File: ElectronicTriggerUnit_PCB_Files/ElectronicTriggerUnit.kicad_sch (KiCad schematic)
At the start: 36 parts, among them IC3 ATTINY816-MNR, J4 Conn_01x04, Q1 LC191PTDT, Q2 LKPT30102B-A01, Q3 78-SQRS140ELP, Q4 LC191PTDT, Q5 2N7002, Q8 SI7149ADP-T1-GE3, U2 12v, U3 GndMotor, U4 Gnd, U5 LM1117MP-5.0

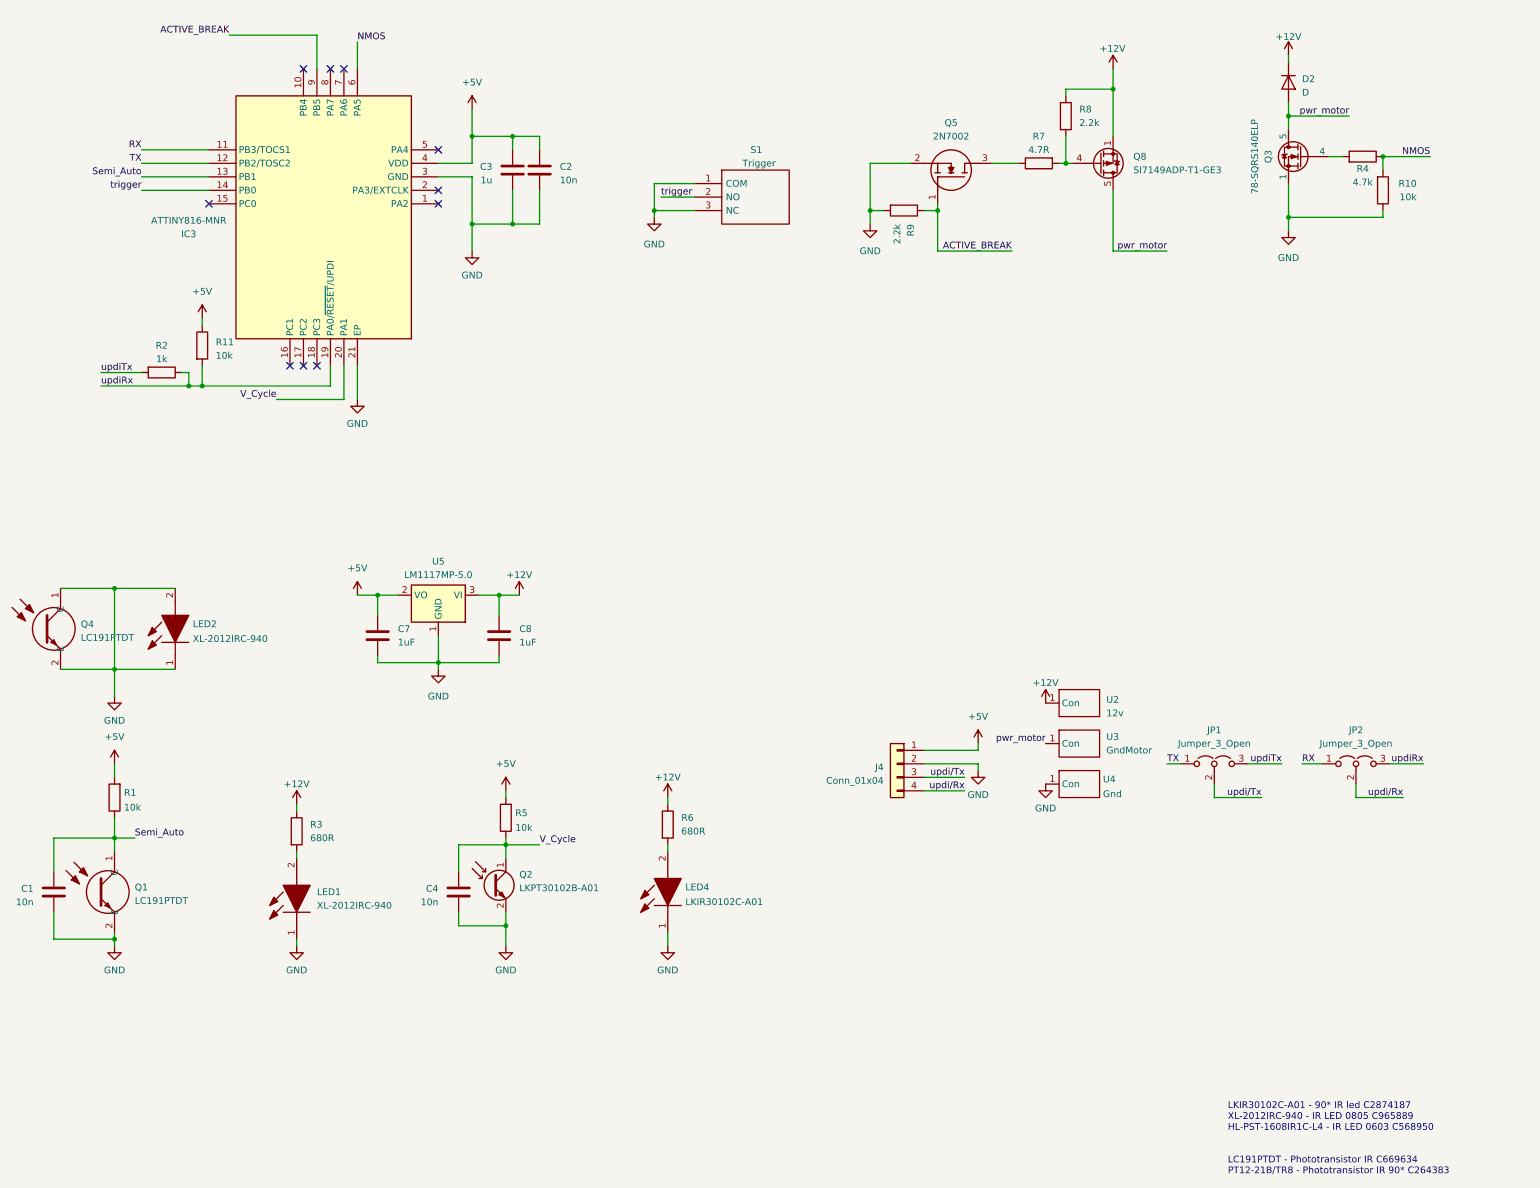
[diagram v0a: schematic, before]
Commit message: modular board version
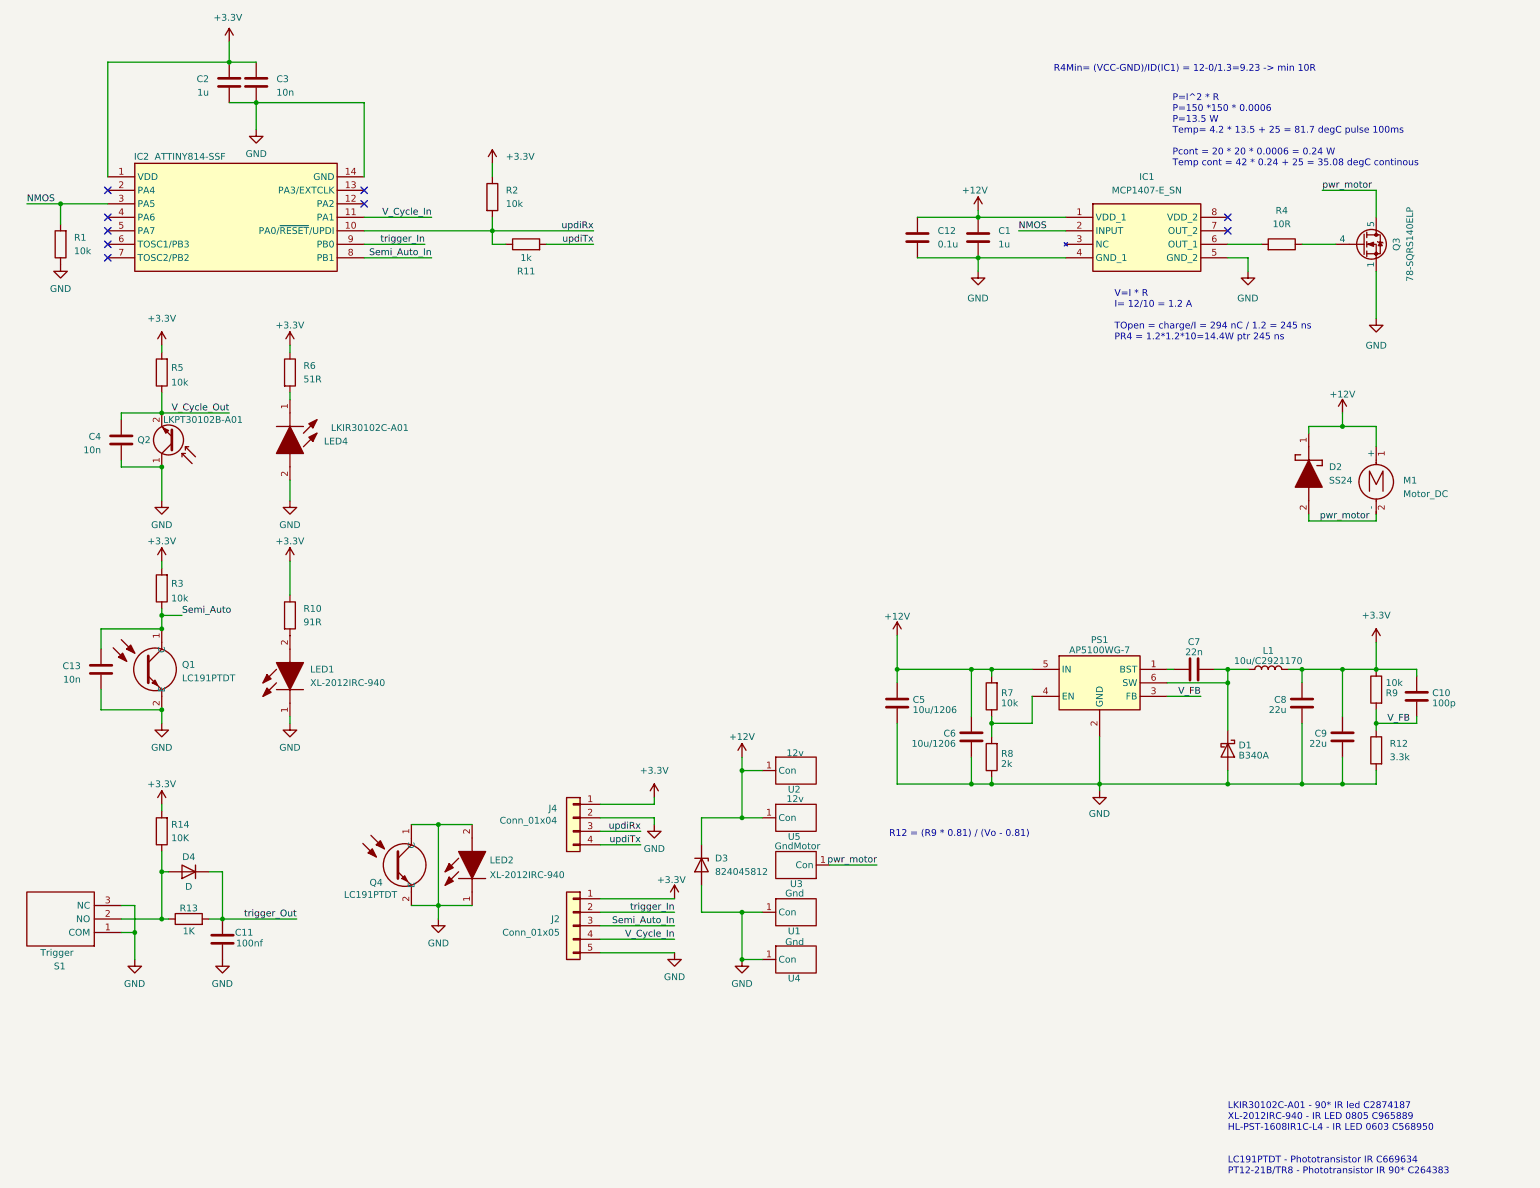
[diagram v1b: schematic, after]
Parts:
- removed D2: D, SamacSys_Parts:SBR3U60P1Q7, symbol Device:D
- removed IC3: ATTINY816-MNR, SamacSys_Parts:QFN40P300X300X90-21N, symbol SamacSys_Parts:ATTINY816-MNR
- removed JP1, JP2: Jumper_3_Open, Jumper:SolderJumper-3_P1.3mm_Open_RoundedPad1.0x1.5mm, symbol Jumper:Jumper_3_Open
- removed Q5: 2N7002, SOT96P240X120-3N, symbol SamacSys_Parts:2N7002
- removed Q8: SI7149ADP-T1-GE3, SamacSys_Parts:POWERPAKSO-8, symbol Transistor_FET:Si7141DP
- removed U5: LM1117MP-5.0, Package_TO_SOT_SMD:SOT-223-3_TabPin2, symbol Regulator_Linear:LM1117MP-5.0
- added C10: 100p, Capacitor_SMD:C_0603_1608Metric, symbol Device:C
- added C11: 100nf, Capacitor_SMD:C_0603_1608Metric, symbol Device:C
- added C12: 0.1u, Capacitor_SMD:C_0603_1608Metric, symbol Device:C
- added C13: 10n, Capacitor_SMD:C_0603_1608Metric, symbol Device:C
- added C5, C6: 10u/1206, Capacitor_SMD:C_0603_1608Metric, symbol Device:C
- added C9: 22u, Capacitor_SMD:C_0603_1608Metric, symbol Device:C
- added D1: B340A, Diode_SMD:D_SMA, symbol Device:D_Schottky
- added D2: SS24, SamacSys:DIOM5436X247N, symbol SamacSys:SS24
- added D3: 824045812, SamacSys:TVS_DIODE, symbol Diode:ESD5Zxx
- added D4: D, Diode_SMD:D_0603_1608Metric, symbol Device:D
- added IC1: MCP1407-E_SN, SamacSys:SOIC127P600X175-8N, symbol SamacSys:MCP1407-E_SN
- added IC2: ATTINY814-SSF, SamacSys:SOIC127P600X175-14N, symbol SamacSys:ATTINY814-SSF
- added J2: Conn_01x05, Connector_PinSocket_2.54mm:PinSocket_1x05_P2.54mm_Vertical, symbol Connector_Generic:Conn_01x05
- added L1: 10u/C2921170, Inductor_SMD:L_Chilisin_BMRA00040420, symbol Device:L
- added M1: Motor_DC, symbol Motor:Motor_DC
- added PS1: AP5100WG-7, SamacSys:SOT95P285X140-6N, symbol SamacSys_Parts:AP5100WG-7
- added R12: 3.3k, Resistor_SMD:R_0603_1608Metric, symbol Device:R
- added R13: 1K, Resistor_SMD:R_0603_1608Metric, symbol Device:R
- added R14: 10K, Resistor_SMD:R_0603_1608Metric, symbol Device:R
- added U1: Gnd, SamacSys:Copper_Pad, symbol Copper_Pad:Copper_pad
- added U5: 12v, SamacSys:Copper_Pad, symbol Copper_Pad:Copper_pad
- C1, C2: value 10n -> 1u; footprint Capacitor_SMD:C_0402_1005Metric -> Capacitor_SMD:C_0603_1608Metric
- C3: value 1u -> 10n; footprint Capacitor_SMD:C_0402_1005Metric -> Capacitor_SMD:C_0603_1608Metric
- C4: footprint Capacitor_SMD:C_0402_1005Metric -> Capacitor_SMD:C_0603_1608Metric
- C7: value 1uF -> 22n; footprint Capacitor_SMD:C_0402_1005Metric -> Capacitor_SMD:C_0603_1608Metric; MPN (none) -> C21122
- C8: value 1uF -> 22u; footprint Capacitor_SMD:C_0402_1005Metric -> Capacitor_SMD:C_0603_1608Metric; MPN (none) -> C45783
- LED1, LED2: footprint SamacSys_Parts:LEDC2012X105N -> SamacSys:LEDC2012X105N
- LED4, Q2: footprint SamacSys_Parts:APA3010P3C -> SamacSys:APA3010P3C
- Q1, Q4: footprint SamacSys_Parts:AP1608P1CP22 -> SamacSys:AP1608P1CP22
- Q3: footprint SamacSys_Parts:POWERPAKSO-8 -> SamacSys:POWERPAKSO-8
- R1, R5: footprint Resistor_SMD:R_0402_1005Metric -> Resistor_SMD:R_0603_1608Metric
- R10: value 10k -> 91R; footprint Resistor_SMD:R_0402_1005Metric -> Resistor_SMD:R_0603_1608Metric
- R11: value 10k -> 1k; footprint Resistor_SMD:R_0402_1005Metric -> Resistor_SMD:R_0603_1608Metric
- R2: value 1k -> 10k; footprint Resistor_SMD:R_0402_1005Metric -> Resistor_SMD:R_0603_1608Metric
- R3: value 680R -> 10k; footprint Resistor_SMD:R_0402_1005Metric -> Resistor_SMD:R_0603_1608Metric
- R4: value 4.7k -> 10R; footprint Resistor_SMD:R_0402_1005Metric -> Resistor_SMD:R_0603_1608Metric
- R6: value 680R -> 51R; footprint Resistor_SMD:R_0402_1005Metric -> Resistor_SMD:R_0603_1608Metric
- R7: value 4.7R -> 10k; footprint Resistor_SMD:R_0402_1005Metric -> Resistor_SMD:R_0603_1608Metric; MPN (none) -> C25804
- R8: value 2.2k -> 2k; footprint Resistor_SMD:R_0402_1005Metric -> Resistor_SMD:R_0603_1608Metric; MPN (none) -> C22975
- R9: value 2.2k -> 10k; footprint Resistor_SMD:R_0402_1005Metric -> Resistor_SMD:R_0603_1608Metric; MPN (none) -> C25804
- S1: footprint SamacSys_Parts:463092691402 -> SamacSys:463092691402
- U2, U3, U4: footprint SamacSys_Parts:Copper_pad -> SamacSys:Copper_Pad
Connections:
- net ACTIVE_BREAK is gone; now on net +3.3V: R9.1
- net updi/Rx is gone; now on net updiTx: J4.4 (Pin_4)
- net updi/Tx is gone; now on net updiRx: J4.3 (Pin_3)
- net +12V: now also C1.2, R7.2, C12.1, C5.1, C6.1, D2.1 (K), D3.1 (K), IC1.1 (VDD_1), M1.1 (+), PS1.5 (IN), U5.1 (Con); no longer C8.2, R3.1, R6.1, R8.1
- net GND: now also C1.1, C8.2, LED4.2, Q2.1 (C), R1.1, R8.1, C11.1, C12.2, C13.2, C5.2, C6.2, C9.2, D1.2 (A), D3.2 (A), IC1.4 (GND_1), IC1.5 (GND_2), IC2.14 (GND), J2.5 (Pin_5), PS1.2 (GND), R12.2, U1.1 (Con); no longer C1.2, C7.1, C8.1, LED4.1, Q2.2 (E), R10.1, R9.2
- net NMOS: now also R1.2, IC1.2 (INPUT), IC2.3 (PA5); no longer R10.2, R4.1
- net Semi_Auto: now also R3.1, C13.1; no longer C1.1, R1.1
- net pwr_motor: now also D2.2 (A), M1.2 (-)
- net updiRx: now also R11.1, R2.2, IC2.10 (PA0/~{RESET}/UPDI); no longer R11.2, R2.1
- net updiTx: now also R11.2; no longer R2.2
- net at LED1.2: now also R10.2; no longer R3.2
- net at R6.2: now also LED4.1; no longer LED4.2
- net at Q3.4: now also R4.1; no longer R4.2
- net at R7.1: now also R8.2, PS1.4 (EN)
- net +5V renamed +3.3V
- net +3.3V: now also C8.1, R10.1, R2.1, R3.2, R6.1, C10.1, C9.1, IC2.1 (VDD), J2.1 (Pin_1), L1.2, R14.2; no longer C7.2, R1.2, R11.1
- net V_Cycle renamed V_Cycle_Out
- net V_Cycle_Out: now also Q2.2 (E); no longer Q2.1 (C)
- net trigger: no longer names the net of S1.2 (NO)
- net trigger: now also D4.2 (A), R13.1, R14.1
- new net: C7.1, PS1.1 (BST)
- new net: C7.2, D1.1 (K), L1.1, PS1.6 (SW)
- new net: IC1.6 (OUT_1), R4.2
- new net Semi_Auto_In: IC2.8 (PB1), J2.3 (Pin_3)
- new net V_Cycle_In: IC2.11 (PA1), J2.4 (Pin_4)
- new net V_FB: C10.2, PS1.3 (FB), R12.1, R9.2
- new net trigger_In: IC2.9 (PB0), J2.2 (Pin_2)
- new net trigger_Out: C11.2, D4.1 (K), R13.2
- no-connect marks 10 -> 9
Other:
- note added: "P=I^2 * R P=150 *150 * 0.0006 P=13.5 W Temp= 4.2 * 13.5 + 25 = 81.7 degC pulse 100ms Pcont = 20 * 20 * 0.0006 = 0.24 W Temp cont = 42 * 0.24 + 25 = 35.08 degC continous"
- note added: "R12 = (R9 * 0.81) / (Vo - 0.81)"
- note added: "R4Min= (VCC-GND)/ID(IC1) = 12-0/1.3=9.23 -> min 10R"
- note added: "V=I * R I= 12/10 = 1.2 A TOpen = charge/I = 294 nC / 1.2 = 245 ns PR4 = 1.2*1.2*10=14.4W ptr 245 ns"
- moved on the sheet: C4, J4, LED4, Q2, Q3, R4, R5, R6, S1, U2, U3, U4
